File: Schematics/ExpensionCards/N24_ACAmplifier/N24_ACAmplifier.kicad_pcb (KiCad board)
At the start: 2 copper layers, 97 x 76 mm, 12 parts

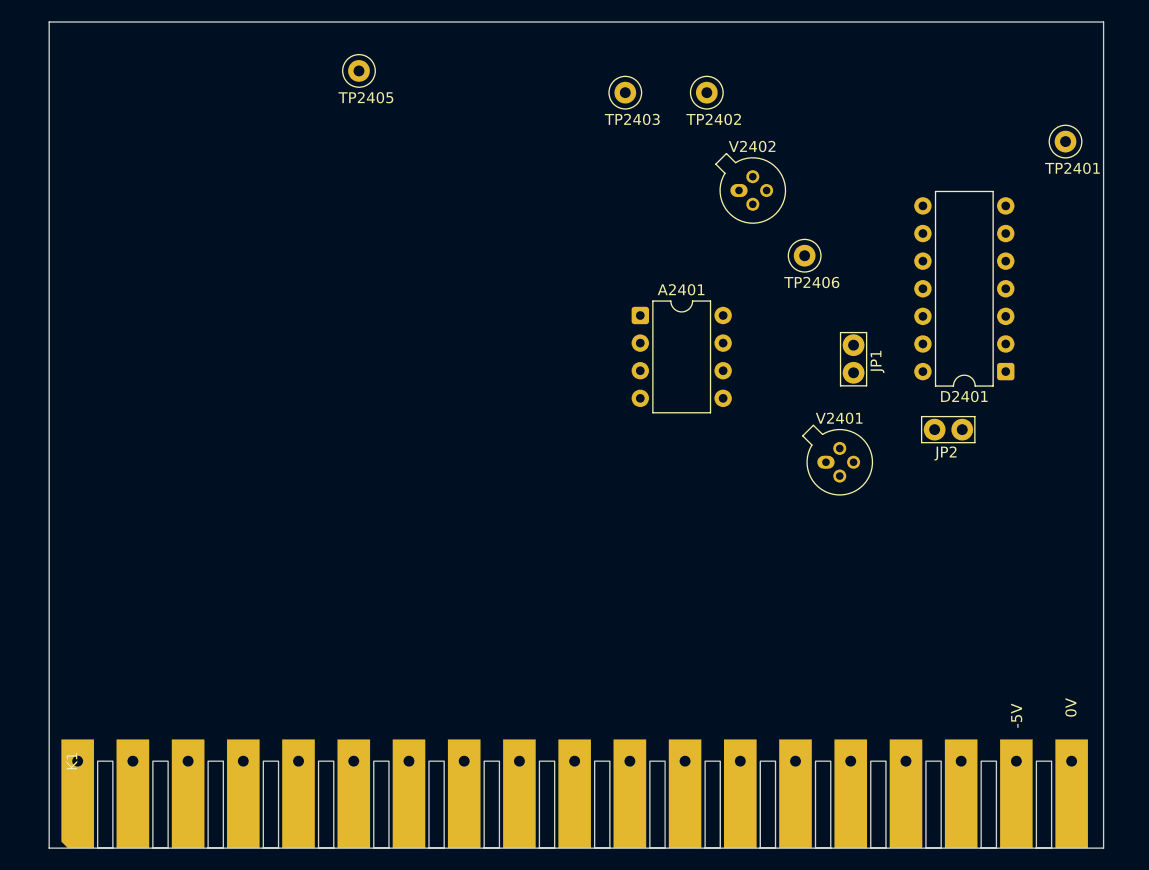
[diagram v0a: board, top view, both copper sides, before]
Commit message: Reworked N20/N21
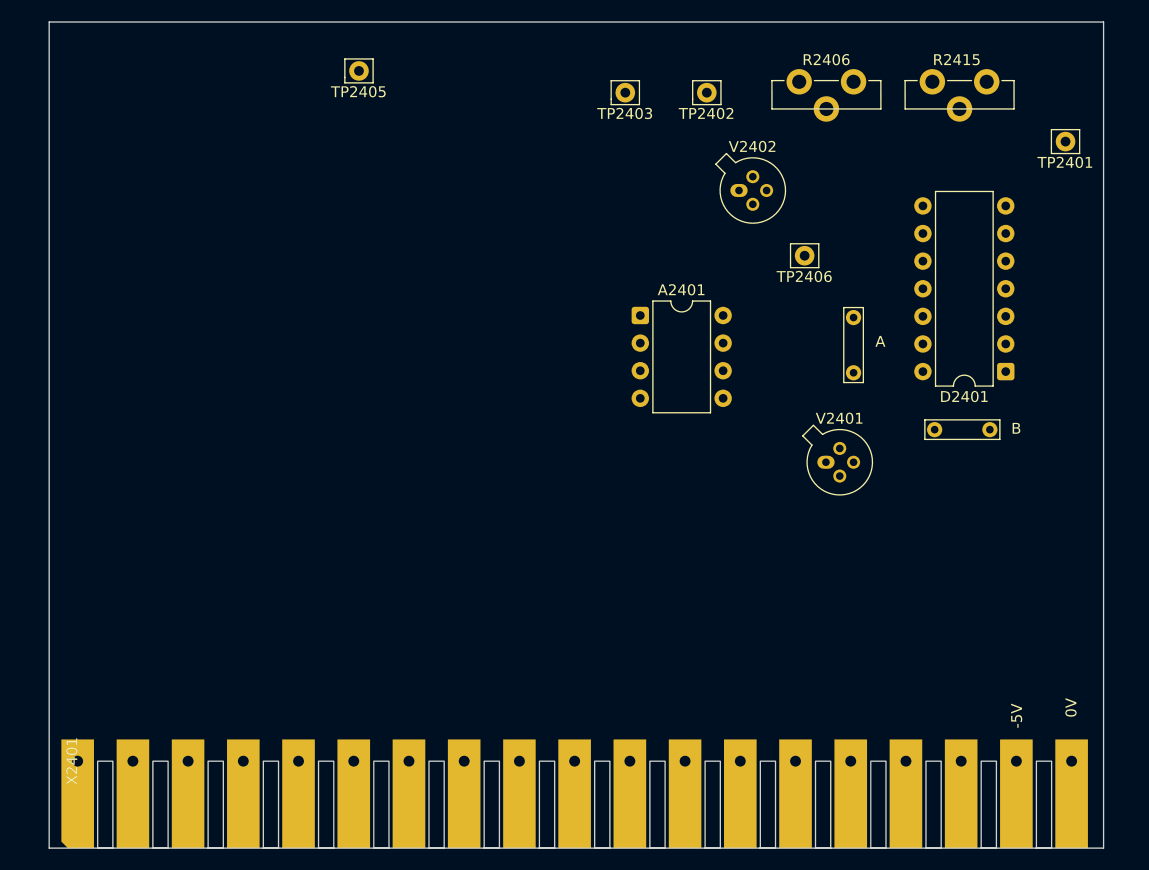
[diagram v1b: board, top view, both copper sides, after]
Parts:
- added R2406: 220k, PM2528:Trimmer vertical, F.Cu at (173.0, 84.0)
- added R2415: 1k, PM2528:Trimmer vertical, F.Cu at (185.2, 84.0)
- JP2401: renamed from JP1; footprint TestPoint:TestPoint_Bridge_Pitch2.54mm_Drill1.0mm -> TestPoint:TestPoint_Bridge_Pitch5.08mm_Drill0.7mm
- JP2402: renamed from JP2; footprint TestPoint:TestPoint_Bridge_Pitch2.54mm_Drill1.0mm -> TestPoint:TestPoint_Bridge_Pitch5.08mm_Drill0.7mm
- TP2401, TP2402, TP2403, TP2405, TP2406: footprint TestPoint:TestPoint_Loop_D2.50mm_Drill1.0mm -> Connector_Pin:Pin_D0.9mm_L10.0mm_W2.4mm_FlatFork
- renumbered K1 to X2401
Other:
- board text added: "A"
- board text added: "B"

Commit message: Updated N24 schema/PCB
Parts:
- added A2402: LM393N, Package_DIP:DIP-8_W7.62mm, F.Cu at (114.1, 122.5)
- added C2401: 22n, Capacitor_THT:C_Rect_L13.0mm_W4.0mm_P10.00mm_FKS3_FKP3_MKS4, F.Cu at (161.2, 139.5)
- added C2402: 8p2, Capacitor_THT:C_Disc_D4.3mm_W1.9mm_P5.00mm, F.Cu at (175.3, 123.8)
- added C2403: 33n, Capacitor_THT:C_Rect_L13.0mm_W4.0mm_P10.00mm_FKS3_FKP3_MKS4, F.Cu at (168.8, 137.0)
- added C2404: 220p, Capacitor_THT:C_Disc_D4.3mm_W1.9mm_P5.00mm, F.Cu at (157.5, 114.8)
- added C2405: 3p9, Capacitor_THT:C_Disc_D4.3mm_W1.9mm_P5.00mm, F.Cu at (159.9, 111.5)
- added C2406: 220n, Capacitor_THT:C_Rect_L13.0mm_W4.0mm_P10.00mm_FKS3_FKP3_MKS4, F.Cu at (164.0, 109.5)
- added C2407: 22u, Capacitor_THT:CP_Radial_Tantal_D4.5mm_P5.00mm, F.Cu at (157.2, 101.5)
- added C2408: 13n3, Capacitor_THT:C_Axial_L5.1mm_D3.1mm_P15.00mm_Horizontal, F.Cu at (192.0, 137.9)
- added C2409: 6u8, Capacitor_THT:CP_Radial_Tantal_D4.5mm_P5.00mm, F.Cu at (180.5, 134.5)
- added C2410: 6u8, Capacitor_THT:CP_Radial_Tantal_D4.5mm_P5.00mm, F.Cu at (185.2, 134.5)
- added C2411: 330n, Capacitor_THT:C_Rect_L18.0mm_W5.0mm_P15.00mm_FKS3_FKP3, F.Cu at (151.0, 125.0)
- added C2412: 150p, Capacitor_THT:C_Disc_D4.3mm_W1.9mm_P5.00mm, F.Cu at (144.8, 119.2)
- added C2413: 10n, Capacitor_THT:C_Disc_D4.3mm_W1.9mm_P5.00mm, F.Cu at (185.5, 129.8)
- added C2414: 1n8, Capacitor_THT:C_Disc_D4.3mm_W1.9mm_P5.00mm, F.Cu at (142.2, 104.0)
- added C2415: 15p, Capacitor_THT:C_Disc_D4.3mm_W1.9mm_P5.00mm, F.Cu at (129.8, 127.2)
- added C2416: 12p, Capacitor_THT:C_Disc_D4.3mm_W1.9mm_P5.00mm, F.Cu at (116.8, 114.0)
- added C2417: 10n, Capacitor_THT:C_Disc_D4.3mm_W1.9mm_P5.00mm, F.Cu at (107.0, 120.8)
- added C2418: 560p, Capacitor_THT:C_Disc_D4.3mm_W1.9mm_P5.00mm, F.Cu at (106.8, 130.0)
- added C2419: 6n8, Capacitor_THT:C_Disc_D4.3mm_W1.9mm_P5.00mm, F.Cu at (109.2, 142.5)
- added C2420: 6n8, Capacitor_THT:C_Disc_D4.3mm_W1.9mm_P5.00mm, F.Cu at (101.5, 142.8)
- added C2421: 22n, Capacitor_THT:C_Disc_D4.3mm_W1.9mm_P5.00mm, F.Cu at (177.8, 143.0)
- added C2422: 22n, Capacitor_THT:C_Disc_D4.3mm_W1.9mm_P5.00mm, F.Cu at (169.0, 142.2)
- added C2423: 22n, Capacitor_THT:C_Disc_D4.3mm_W1.9mm_P5.00mm, F.Cu at (119.5, 107.2)
- added C2424: 22n, Capacitor_THT:C_Disc_D4.3mm_W1.9mm_P5.00mm, F.Cu at (132.5, 111.5)
- added C2425: 39p, Capacitor_THT:C_Disc_D4.3mm_W1.9mm_P5.00mm, F.Cu at (116.8, 120.8)
- added JP1: Jumper_2_Small_Bridged, TestPoint:TestPoint_Bridge_Pitch5.08mm_Drill0.7mm, F.Cu at (132.5, 104.3)
- added R2401: 1M00, Resistor_THT:R_Axial_DIN0207_L6.3mm_D2.5mm_P10.16mm_Horizontal, F.Cu at (157.8, 140.8)
- added R2402: 95k3, Resistor_THT:R_Axial_DIN0207_L6.3mm_D2.5mm_P10.16mm_Horizontal, F.Cu at (165.2, 141.5)
- added R2403: 9k53, Resistor_THT:R_Axial_DIN0207_L6.3mm_D2.5mm_P10.16mm_Horizontal, F.Cu at (157.5, 127.2)
- added R2404: 15E4, Resistor_THT:R_Axial_DIN0207_L6.3mm_D2.5mm_P10.16mm_Horizontal, F.Cu at (175.5, 139.5)
- added R2405: 681k, Resistor_THT:R_Axial_DIN0207_L6.3mm_D2.5mm_P10.16mm_Horizontal, F.Cu at (178.0, 121.2)
- added R2407: 1M00, Resistor_THT:R_Axial_DIN0207_L6.3mm_D2.5mm_P10.16mm_Horizontal, F.Cu at (172.5, 139.5)
- added R2408: 681k, Resistor_THT:R_Axial_DIN0207_L6.3mm_D2.5mm_P10.16mm_Horizontal, F.Cu at (170.0, 121.8)
- added R2409: 2k74, Resistor_THT:R_Axial_DIN0207_L6.3mm_D2.5mm_P10.16mm_Horizontal, F.Cu at (173.0, 121.5)
- added R2410: 15k4, Resistor_THT:R_Axial_DIN0207_L6.3mm_D2.5mm_P10.16mm_Horizontal, F.Cu at (167.8, 109.5)
- added R2411: 1M00, Resistor_THT:R_Axial_DIN0207_L6.3mm_D2.5mm_P10.16mm_Horizontal, F.Cu at (160.2, 109.5)
- added R2412: 1k05, Resistor_THT:R_Axial_DIN0207_L6.3mm_D2.5mm_P10.16mm_Horizontal, F.Cu at (183.1, 121.1)
- added R2413: 634k, Resistor_THT:R_Axial_DIN0207_L6.3mm_D2.5mm_P10.16mm_Horizontal, F.Cu at (188.0, 134.5)
- added R2414: 17k8, Resistor_THT:R_Axial_DIN0207_L6.3mm_D2.5mm_P10.16mm_Horizontal, F.Cu at (183.0, 109.2)
- added R2416: 1k21, Resistor_THT:R_Axial_DIN0207_L6.3mm_D2.5mm_P10.16mm_Horizontal, F.Cu at (180.2, 109.2)
- added R2417: 10M, Resistor_THT:R_Axial_DIN0207_L6.3mm_D2.5mm_P10.16mm_Horizontal, F.Cu at (147.2, 142.4)
- added R2418: 46k4, Resistor_THT:R_Axial_DIN0207_L6.3mm_D2.5mm_P10.16mm_Horizontal, F.Cu at (144.8, 109.0)
- added R2419: 46k4, Resistor_THT:R_Axial_DIN0207_L6.3mm_D2.5mm_P10.16mm_Horizontal, F.Cu at (147.5, 111.5)
- added R2420: 8k25, Resistor_THT:R_Axial_DIN0207_L6.3mm_D2.5mm_P10.16mm_Horizontal, F.Cu at (137.3, 127.3)
- added R2421: 8k25, Resistor_THT:R_Axial_DIN0207_L6.3mm_D2.5mm_P10.16mm_Horizontal, F.Cu at (140.0, 129.5)
- added R2422: 150, PM2528:Trimmer vertical, F.Cu at (150.2, 96.5)
- added R2423: 46k4, Resistor_THT:R_Axial_DIN0207_L6.3mm_D2.5mm_P10.16mm_Horizontal, F.Cu at (150.2, 108.8)
- added R2424: 10k, Resistor_THT:R_Axial_DIN0207_L6.3mm_D2.5mm_P10.16mm_Horizontal, F.Cu at (152.8, 111.2)
- added R2425: 2k74, Resistor_THT:R_Axial_DIN0207_L6.3mm_D2.5mm_P10.16mm_Horizontal, F.Cu at (142.2, 119.8)
- added R2426: 1k78, Resistor_THT:R_Axial_DIN0207_L6.3mm_D2.5mm_P10.16mm_Horizontal, F.Cu at (137.0, 106.3)
- added R2427: 140, Resistor_THT:R_Axial_DIN0207_L6.3mm_D2.5mm_P10.16mm_Horizontal, F.Cu at (139.8, 106.5)
- added R2428: 10M, Resistor_THT:R_Axial_DIN0207_L6.3mm_D2.5mm_P10.16mm_Horizontal, F.Cu at (127.2, 129.5)
- added R2429: 301k, Resistor_THT:R_Axial_DIN0207_L6.3mm_D2.5mm_P10.16mm_Horizontal, F.Cu at (132.5, 129.5)
- added R2430: 60k4, Resistor_THT:R_Axial_DIN0207_L6.3mm_D2.5mm_P10.16mm_Horizontal, F.Cu at (129.8, 112.0)
- added R2431: 2k15, Resistor_THT:R_Axial_DIN0207_L6.3mm_D2.5mm_P10.16mm_Horizontal, F.Cu at (127.2, 114.0)
- added R2432: 205, Resistor_THT:R_Axial_DIN0207_L6.3mm_D2.5mm_P10.16mm_Horizontal, F.Cu at (114.5, 111.5)
- added R2433: 2k61, Resistor_THT:R_Axial_DIN0207_L6.3mm_D2.5mm_P10.16mm_Horizontal, F.Cu at (112.0, 129.5)
- added R2434: 2k37, Resistor_THT:R_Axial_DIN0207_L6.3mm_D2.5mm_P10.16mm_Horizontal, F.Cu at (117.0, 106.2)
- added R2435: 7R05, Resistor_THT:R_Axial_DIN0207_L6.3mm_D2.5mm_P10.16mm_Horizontal, F.Cu at (111.9, 113.9)
- added R2436: 7R05, Resistor_THT:R_Axial_DIN0207_L6.3mm_D2.5mm_P10.16mm_Horizontal, F.Cu at (109.8, 106.5)
- added R2437: 2k15, Resistor_THT:R_Axial_DIN0207_L6.3mm_D2.5mm_P10.16mm_Horizontal, F.Cu at (122.2, 106.5)
- added R2438: 4k64, Resistor_THT:R_Axial_DIN0207_L6.3mm_D2.5mm_P10.16mm_Horizontal, F.Cu at (104.5, 115.2)
- added R2439: 215, Resistor_THT:R_Axial_DIN0207_L6.3mm_D2.5mm_P10.16mm_Horizontal, F.Cu at (101.5, 113.0)
- added R2440: 71R5, Resistor_THT:R_Axial_DIN0207_L6.3mm_D2.5mm_P10.16mm_Horizontal, F.Cu at (109.2, 132.0)
- added R2441: 71R5, Resistor_THT:R_Axial_DIN0207_L6.3mm_D2.5mm_P10.16mm_Horizontal, F.Cu at (101.2, 132.0)
- added R2442: 21R15, Resistor_THT:R_Axial_DIN0207_L6.3mm_D2.5mm_P10.16mm_Horizontal, F.Cu at (104.2, 129.8)
- added R2443: 71R5, Resistor_THT:R_Axial_DIN0207_L6.3mm_D2.5mm_P10.16mm_Horizontal, F.Cu at (114.5, 142.2)
- added R2444: 71R5, Resistor_THT:R_Axial_DIN0207_L6.3mm_D2.5mm_P10.16mm_Horizontal, F.Cu at (106.8, 142.2)
- added R2445: 1k05, Resistor_THT:R_Axial_DIN0207_L6.3mm_D2.5mm_P10.16mm_Horizontal, F.Cu at (183.0, 134.0)
- added R2446: 1k21, Resistor_THT:R_Axial_DIN0207_L6.3mm_D2.5mm_P10.16mm_Horizontal, F.Cu at (137.2, 142.0)
- added R2447: 15k4, Resistor_THT:R_Axial_DIN0207_L6.3mm_D2.5mm_P10.16mm_Horizontal, F.Cu at (122.0, 142.5)
- added R2448: 15k4, Resistor_THT:R_Axial_DIN0207_L6.3mm_D2.5mm_P10.16mm_Horizontal, F.Cu at (124.5, 142.5)
- added R2449: 46k4, Resistor_THT:R_Axial_DIN0207_L6.3mm_D2.5mm_P10.16mm_Horizontal, F.Cu at (124.5, 129.5)
- added R2450: 30k1, Resistor_THT:R_Axial_DIN0207_L6.3mm_D2.5mm_P10.16mm_Horizontal, F.Cu at (127.2, 142.5)
- added R2451: 1k05, Resistor_THT:R_Axial_DIN0207_L6.3mm_D2.5mm_P10.16mm_Horizontal, F.Cu at (124.5, 116.7)
- added R2452: 1k05, Resistor_THT:R_Axial_DIN0207_L6.3mm_D2.5mm_P10.16mm_Horizontal, F.Cu at (122.2, 118.5)
- added R2453: 30k1, Resistor_THT:R_Axial_DIN0207_L6.3mm_D2.5mm_P10.16mm_Horizontal, F.Cu at (119.5, 119.0)
- added TP2404: something, Connector_Pin:Pin_D0.9mm_L10.0mm_W2.4mm_FlatFork, F.Cu at (131.0, 96.8)
- added TP2407: OUT, Connector_Pin:Pin_D0.9mm_L10.0mm_W2.4mm_FlatFork, F.Cu at (103.8, 132.2)
- added V2404: BFQ14, Package_TO_SOT_THT:TO-75-6, F.Cu at (148.9, 119.2)
- added V2405: BC547B, Package_TO_SOT_THT:TO-92_Inline, F.Cu at (142.7, 122.5)
- added V2406: BC547B, Package_TO_SOT_THT:TO-92_Inline, F.Cu at (144.2, 127.7)
- added V2407: BC557B, Package_TO_SOT_THT:TO-92_Inline, F.Cu at (137.7, 115.0)
- added V2408: BC557B, Package_TO_SOT_THT:TO-92_Inline, F.Cu at (137.5, 109.2)
- added V2409: BFW11, Package_TO_SOT_THT:TO-72-4, F.Cu at (128.2, 117.5)
- added V2410: BFW11, Package_TO_SOT_THT:TO-72-4, F.Cu at (126.0, 99.5)
- added V2411: BF199, Package_TO_SOT_THT:TO-92_Inline, F.Cu at (112.0, 117.0)
- added V2412: BF199, Package_TO_SOT_THT:TO-92_Inline, F.Cu at (112.5, 96.5)
- added V2413: BC547B, Package_TO_SOT_THT:TO-92_Inline, F.Cu at (102.2, 100.7)
- added V2415: BF199, Package_TO_SOT_THT:TO-92_Inline, F.Cu at (110.0, 134.5)
- added V2416: BF324, Package_TO_SOT_THT:TO-92_Inline, F.Cu at (102.0, 135.0)
- added V2417: BZX79-C3V0, Diode_THT:D_DO-35_SOD27_P10.16mm_Horizontal, F.Cu at (106.8, 101.8)
- added V2418: BZV46-C2V0, Diode_THT:D_DO-35_SOD27_P10.16mm_Horizontal, F.Cu at (109.5, 109.9)
- added V2419: BAV45, Package_TO_SOT_THT:TO-72-4, F.Cu at (143.8, 133.5)
- added V2420: BAV45, Package_TO_SOT_THT:TO-72-4, F.Cu at (141.2, 139.8)
- added V2421: BAW62, Diode_THT:D_DO-35_SOD27_P10.16mm_Horizontal, F.Cu at (132.2, 142.3)
- added V2422: BAW62, Diode_THT:D_DO-35_SOD27_P10.16mm_Horizontal, F.Cu at (129.8, 142.3)
- added V2423: BZX79-B8V2, Diode_THT:D_DO-35_SOD27_P10.16mm_Horizontal, F.Cu at (119.5, 132.4)
- added V2424: BZX79-B8V2, Diode_THT:D_DO-35_SOD27_P10.16mm_Horizontal, F.Cu at (117.0, 142.3)
- moved TP2405 16.0 mm to (119.2, 96.8)
- moved V2402 14.2 mm to (171.7, 104.8)
- moved TP2402 14.1 mm to (168.0, 96.2)
- moved TP2403 14.0 mm to (160.0, 96.5)
- moved R2406 13.5 mm to (178.0, 96.5)
- moved R2415 12.7 mm to (189.5, 96.0)
- moved TP2406 11.7 mm to (175.2, 109.5)
- moved JP2401 11.4 mm to (180.5, 119.3)
- moved A2401 11.2 mm to (160.1, 114.5)
- moved TP2401 10.9 mm to (195.5, 100.0)
- moved D2401 10.6 mm to (193.0, 119.4)
- moved V2401 10.2 mm to (176.5, 127.2)
- moved JP2402 6.95 mm to (184.0, 122.0)
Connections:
- TP2402 pad 1: Net-(V2402-S) -> Net-(V2402-D)
- V2402 pad 2: Net-(V2402-S) -> GND4
- V2402 pad 3: GND4 -> Net-(V2402-D)
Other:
- board size 97 x 76 mm -> 101.5 x 63 mm
- board text added: "0V"
- board text added: "Fchop"
- board text added: "Ioff"
- board text added: "Out"
- board text added: "Spike"
- board text added: "Voff"

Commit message: Updated some component-values
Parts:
- R2404: value 15E4 -> 15R4
- R2435, R2436: value 7R05 -> 7R5
- R2447: value 15k4 -> 15K4
- TP2401: value V.Chopper -> Fchop
- V2418: value BZV46-C2V0 -> BZX46-C2V0
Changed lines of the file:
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@@
 	(title_block
 		(title "Philips PM2528 - N24 (AC Amplifier)")
-		(date "2025-08-15")
+		(date "2025-08-17")
 		(rev "1.0")
 		(company "D. Kupers")
@@
 			)
 		)
-		(property "Value" "7R05"
+		(property "Value" "7R5"
 			(at 5.08 2.37 90)
 			(layer "F.Fab")
@@
 			)
 		)
-		(property "Value" "BZV46-C2V0"
+		(property "Value" "BZX46-C2V0"
 			(at 5.08 2.12 270)
 			(layer "F.Fab")
@@
 			)
 		)
-		(property "Value" "7R05"
+		(property "Value" "7R5"
 			(at 5.08 2.37 90)
 			(layer "F.Fab")
@@
 			)
 		)
-		(property "Value" "V.Chopper"
+		(property "Value" "Fchop"
 			(at 0 -2.05 0)
 			(layer "F.Fab")
@@
 			)
 		)
-		(property "Value" "15E4"
+		(property "Value" "15R4"
 			(at 5.08 2.37 90)
 			(layer "F.Fab")
@@
 			)
 		)
-		(property "Value" "15k4"
+		(property "Value" "15K4"
 			(at 5.08 2.37 90)
 			(layer "F.Fab")
